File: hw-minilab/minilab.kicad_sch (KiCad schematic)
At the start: 67 parts, among them J1 Screw_Terminal_01x02, J10 Screw_Terminal_01x03, J11 Screw_Terminal_01x03, J12 Conn_01x09_Male, J2 Screw_Terminal_01x02, J3 Conn_01x09_Male, J4 Screw_Terminal_01x04, J5 Screw_Terminal_01x03, J6 Screw_Terminal_01x03, J7 Screw_Terminal_01x03, J8 Screw_Terminal_01x03, J9 Screw_Terminal_01x03, SW1 SW_DPDT_x2, SW2 SW_SPDT, U1 NE555P, U2 L7805, U3 L7833, U4 4069, U5 4069

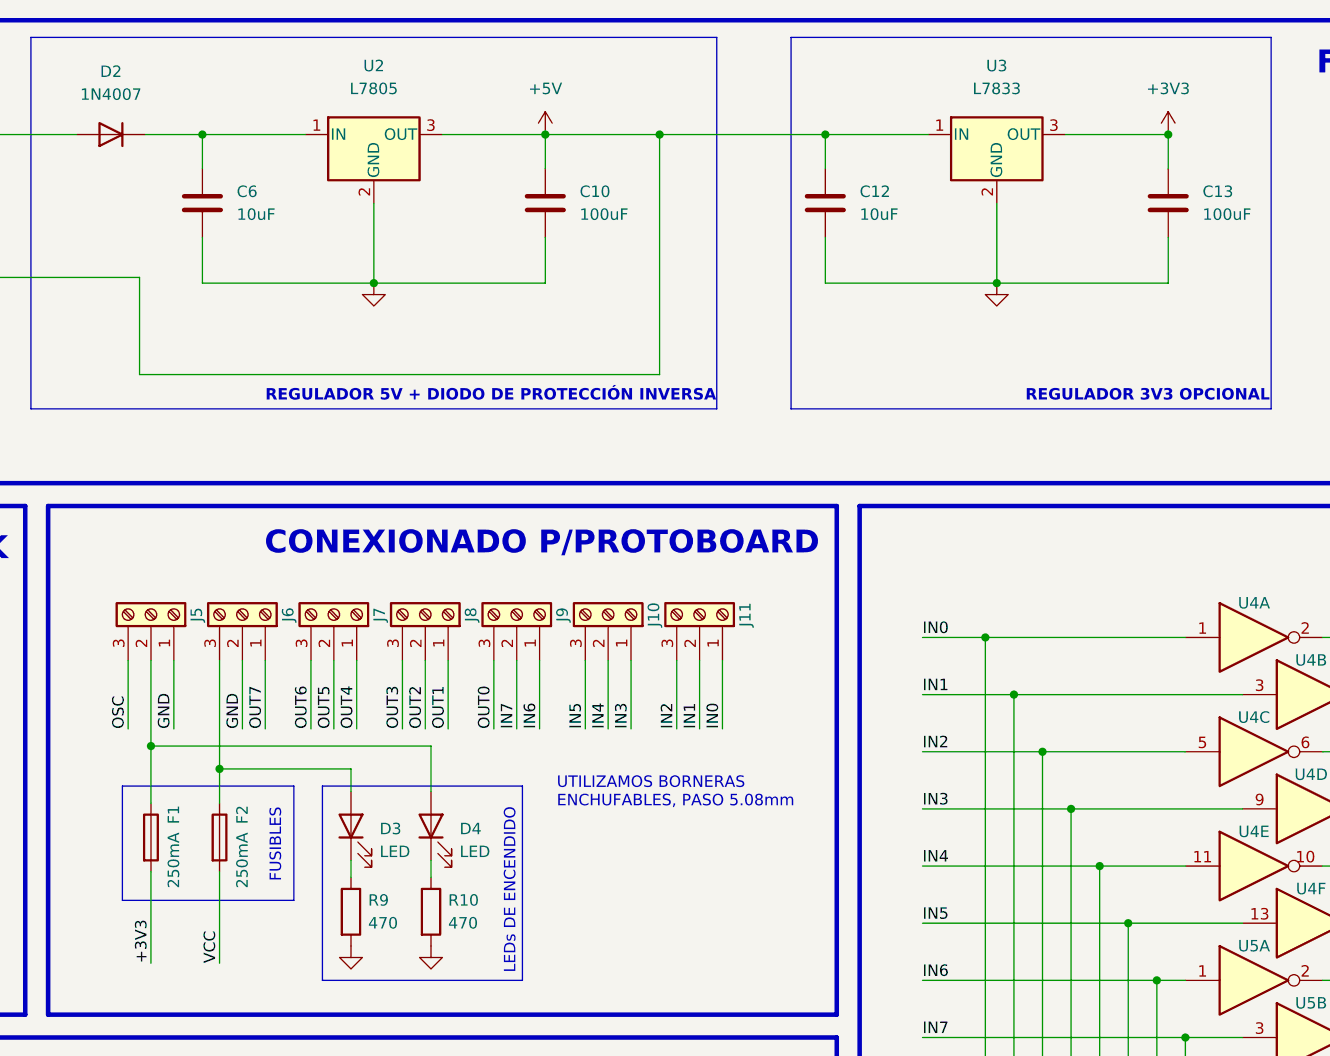
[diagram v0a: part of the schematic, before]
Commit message: Switch 3v3 regulator to kf33
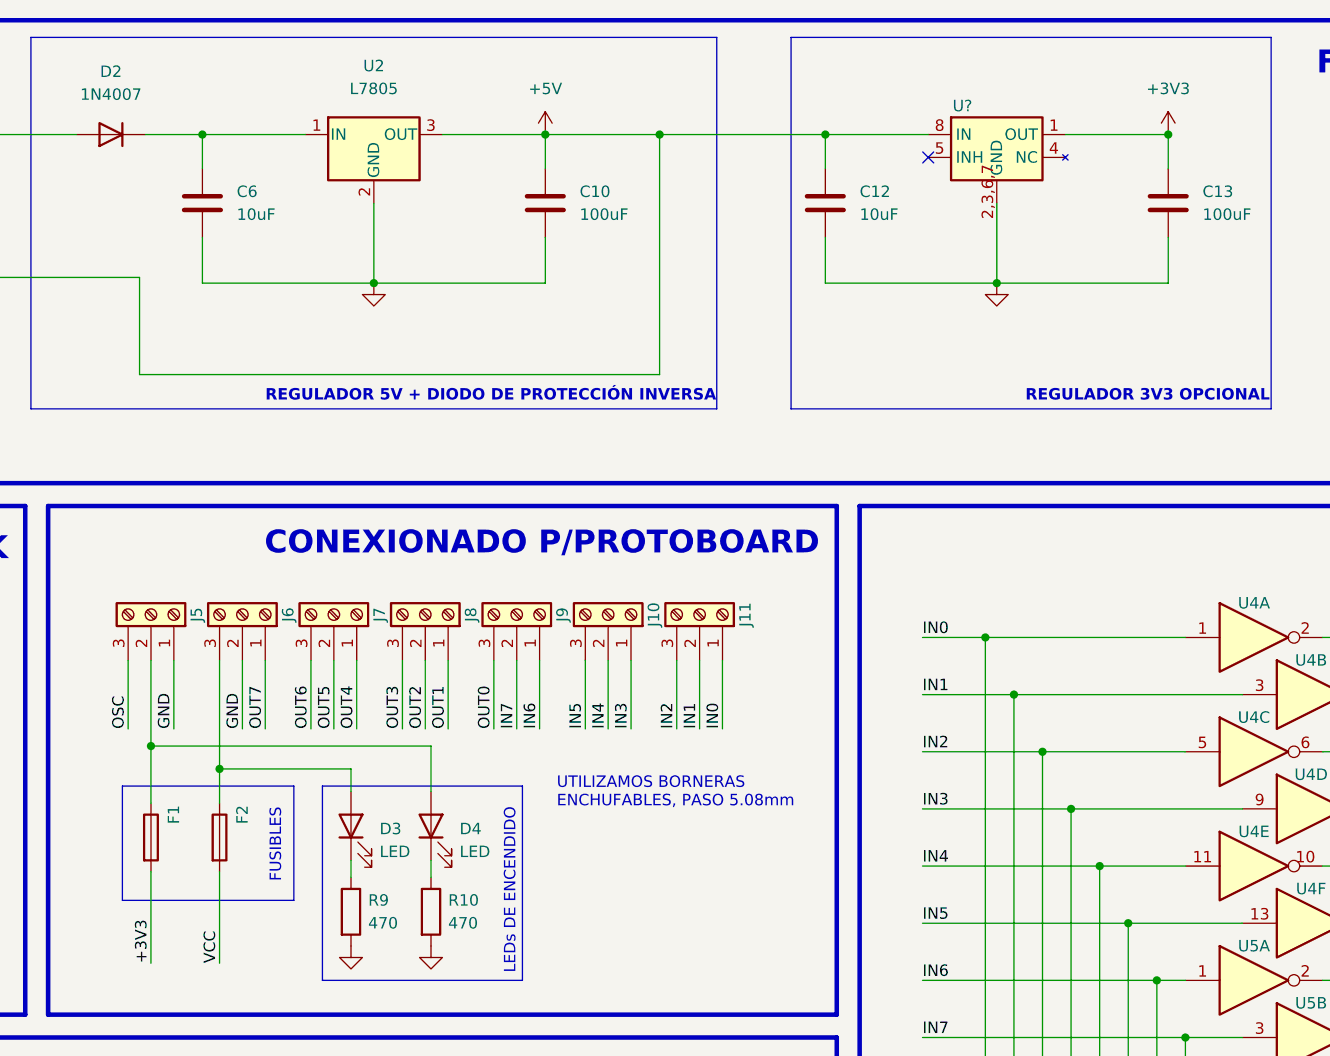
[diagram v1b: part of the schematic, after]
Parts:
- removed U3: L7833, Package_TO_SOT_THT:TO-220-3_Vertical, symbol Regulator_Linear:L7805
- added U?: (no value), symbol lib:KF33
- F1, F2: value 250mA -> (none); footprint TerminalBlock_RND:TerminalBlock_RND_205-00288_1x02_P5.08mm_Horizontal -> (none)
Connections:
- net +3V3: now also U?.1 (OUT)
- net +5V: now also U?.8 (IN)
- net GND: now also U?.2,3,6,7 (GND)
- no-connect marks 3 -> 4
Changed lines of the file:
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@@
   (no_connect (at 53.34 100.965))
   (no_connect (at 27.94 95.885))
+  (no_connect (at 184.785 29.21))
   (no_connect (at 63.5 29.21))
   (polyline (pts (xy 117.475 99.06) (xy 139.7 99.06))
@@
     (stroke (width 0) (type default) (color 0 0 0 0))
   )
+  (wire (pts (xy 200.025 26.67) (xy 211.455 26.67))
+    (stroke (width 0) (type default) (color 0 0 0 0))
+  )
   (wire (pts (xy 253.365 94.615) (xy 267.97 94.615))
     (stroke (width 0) (type default) (color 0 0 0 0))
@@
     (stroke (width 0) (type default) (color 0 0 0 0))
   )
-  (wire (pts (xy 184.785 26.67) (xy 173.355 26.67))
+  (wire (pts (xy 173.355 26.67) (xy 184.785 26.67))
     (stroke (width 0) (type default) (color 0 0 0 0))
   )
@@
     (stroke (width 0) (type default) (color 0 0 0 0))
   )
-  (wire (pts (xy 211.455 26.67) (xy 200.025 26.67))
-    (stroke (width 0) (type default) (color 0 0 0 0))
-  )
   (wire (pts (xy 248.285 107.95) (xy 243.84 107.95))
     (stroke (width 0) (type default) (color 0 0 0 0))
@@
     (pin "1")
   )
-  (symbol (lib_id "Regulator_Linear:L7805") (at 192.405 26.67 0) (unit 1)
-    (in_bom yes) (on_board yes) (fields_autoplaced)
-    (property "Reference" "U3" (id 0) (at 192.405 19.05 0))
-    (property "Value" "L7833" (id 1) (at 192.405 21.59 0))
-    (property "Footprint" "Package_TO_SOT_THT:TO-220-3_Vertical" (id 2) (at 193.04 30.48 0)
-      (effects (font (size 1.27 1.27) italic) (justify left) hide)
+  (symbol (lib_id "lib:KF33") (at 192.405 26.67 0) (unit 1)
+    (in_bom yes) (on_board yes)
+    (property "Reference" "U?" (id 0) (at 188.595 23.495 0))
+    (property "Value" "" (id 1) (at 194.945 23.495 0))
+    (property "Footprint" "" (id 2) (at 192.405 26.67 0)
+      (effects (font (size 1.27 1.27)) hide)
     )
-    (property "Datasheet" "http://www.st.com/content/ccc/resource/technical/document/datasheet/41/4f/b3/b0/12/d4/47/88/CD00000444.pdf/files/CD00000444.pdf/jcr:content/translations/en.CD00000444.pdf" (id 3) (at 192.405 27.94 0)
+    (property "Datasheet" "" (id 3) (at 192.405 26.67 0)
       (effects (font (size 1.27 1.27)) hide)
     )
+    (pin "4")
     (pin "1")
-    (pin "2")
-    (pin "3")
+    (pin "2,3,6,7")
+    (pin "5")
+    (pin "8")
   )
   (symbol (lib_id "Device:R") (at 240.03 127 90) (unit 1)
@@
     (in_bom yes) (on_board yes)
     (property "Reference" "F1" (id 0) (at 100.965 102.235 90))
-    (property "Value" "250mA" (id 1) (at 100.965 107.315 90))
-    (property "Footprint" "TerminalBlock_RND:TerminalBlock_RND_205-00288_1x02_P5.08mm_Horizontal" (id 2) (at 96.647 104.775 90)
+    (property "Value" "" (id 1) (at 100.965 107.315 90))
+    (property "Footprint" "" (id 2) (at 96.647 104.775 90)
       (effects (font (size 1.27 1.27)) hide)
     )
@@
     (in_bom yes) (on_board yes)
     (property "Reference" "F2" (id 0) (at 108.585 102.235 90))
-    (property "Value" "250mA" (id 1) (at 108.585 107.315 90))
-    (property "Footprint" "TerminalBlock_RND:TerminalBlock_RND_205-00288_1x02_P5.08mm_Horizontal" (id 2) (at 104.267 104.775 90)
+    (property "Value" "" (id 1) (at 108.585 107.315 90))
+    (property "Footprint" "" (id 2) (at 104.267 104.775 90)
       (effects (font (size 1.27 1.27)) hide)
     )
@@
     )
     (path "/a3002aff-87e0-400d-bde0-570e1f15484d"
-      (reference "F1") (unit 1) (value "250mA") (footprint "TerminalBlock_RND:TerminalBlock_RND_205-00288_1x02_P5.08mm_Horizontal")
+      (reference "F1") (unit 1) (value "250mA") (footprint "TerminalBlock_Phoenix:TerminalBlock_Phoenix_MKDS-1,5-2-5.08_1x02_P5.08mm_Horizontal")
     )
     (path "/b7c6bafb-aadf-472c-921e-3a8cb7a59ac2"
-      (reference "F2") (unit 1) (value "250mA") (footprint "TerminalBlock_RND:TerminalBlock_RND_205-00288_1x02_P5.08mm_Horizontal")
+      (reference "F2") (unit 1) (value "250mA") (footprint "TerminalBlock_Phoenix:TerminalBlock_Phoenix_MKDS-1,5-2-5.08_1x02_P5.08mm_Horizontal")
     )
     (path "/2dd780f8-df52-4609-ad66-25501efcd296"
@@
       (reference "U2") (unit 1) (value "L7805") (footprint "Package_TO_SOT_THT:TO-220-3_Vertical")
     )
-    (path "/056a54a7-0913-41c5-a754-b3201ec3b595"
-      (reference "U3") (unit 1) (value "L7833") (footprint "Package_TO_SOT_THT:TO-220-3_Vertical")
-    )
     (path "/f245ec42-7b6c-4ad0-aa95-177eeea6ecef"
       (reference "U4") (unit 1) (value "4069") (footprint "Package_DIP:DIP-14_W7.62mm_Socket_LongPads")
@@
       (reference "U5") (unit 7) (value "4069") (footprint "Package_DIP:DIP-14_W7.62mm_Socket_LongPads")
     )
+    (path "/03a24617-13e6-4922-ab6c-5cb103d61f18"
+      (reference "U?") (unit 1) (value "KF33") (footprint "Package_SO:SOIC-8-1EP_3.9x4.9mm_P1.27mm_EP2.29x3mm")
+    )
   )

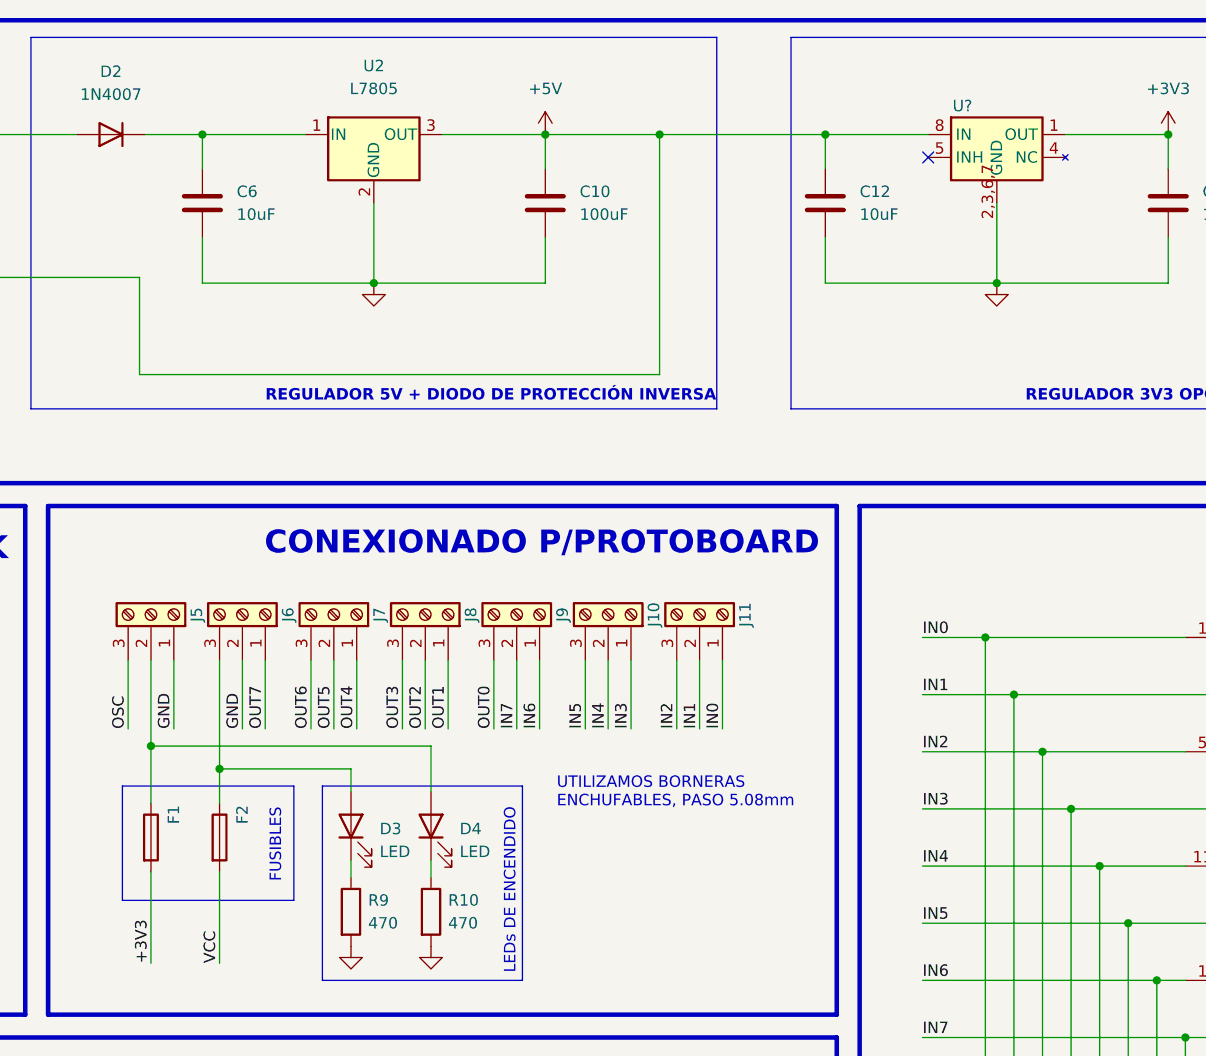
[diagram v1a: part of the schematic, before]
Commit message: Avances en el routeo
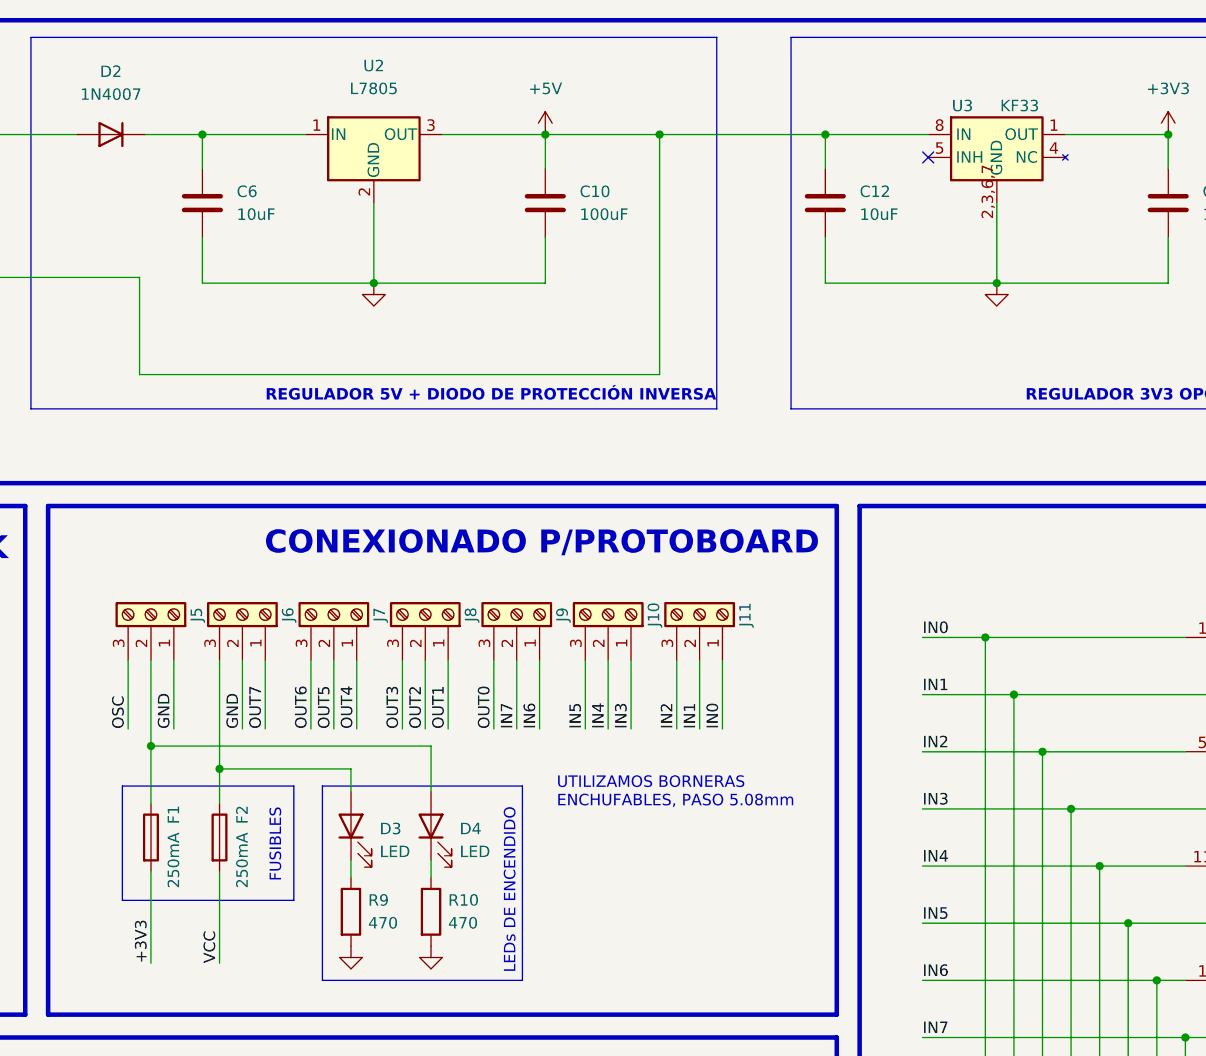
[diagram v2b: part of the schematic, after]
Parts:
- F1, F2: value (none) -> 250mA; footprint (none) -> TerminalBlock_Phoenix:TerminalBlock_Phoenix_MKDS-1,5-2-5.08_1x02_P5.08mm_Horizontal
- U3: renamed from U?; value (none) -> KF33; footprint (none) -> Package_SO:SOIC-8-1EP_3.9x4.9mm_P1.27mm_EP2.29x3mm
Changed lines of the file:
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@@
   (symbol (lib_id "lib:KF33") (at 192.405 26.67 0) (unit 1)
     (in_bom yes) (on_board yes)
-    (property "Reference" "U?" (id 0) (at 188.595 23.495 0))
-    (property "Value" "" (id 1) (at 194.945 23.495 0))
-    (property "Footprint" "" (id 2) (at 192.405 26.67 0)
+    (property "Reference" "U3" (id 0) (at 188.595 23.495 0))
+    (property "Value" "KF33" (id 1) (at 194.945 23.495 0))
+    (property "Footprint" "Package_SO:SOIC-8-1EP_3.9x4.9mm_P1.27mm_EP2.29x3mm" (id 2) (at 192.405 26.67 0)
       (effects (font (size 1.27 1.27)) hide)
     )
@@
     (in_bom yes) (on_board yes)
     (property "Reference" "F1" (id 0) (at 100.965 102.235 90))
-    (property "Value" "" (id 1) (at 100.965 107.315 90))
-    (property "Footprint" "" (id 2) (at 96.647 104.775 90)
+    (property "Value" "250mA" (id 1) (at 100.965 107.315 90))
+    (property "Footprint" "TerminalBlock_Phoenix:TerminalBlock_Phoenix_MKDS-1,5-2-5.08_1x02_P5.08mm_Horizontal" (id 2) (at 96.647 104.775 90)
       (effects (font (size 1.27 1.27)) hide)
     )
@@
     (in_bom yes) (on_board yes)
     (property "Reference" "F2" (id 0) (at 108.585 102.235 90))
-    (property "Value" "" (id 1) (at 108.585 107.315 90))
-    (property "Footprint" "" (id 2) (at 104.267 104.775 90)
+    (property "Value" "250mA" (id 1) (at 108.585 107.315 90))
+    (property "Footprint" "TerminalBlock_Phoenix:TerminalBlock_Phoenix_MKDS-1,5-2-5.08_1x02_P5.08mm_Horizontal" (id 2) (at 104.267 104.775 90)
       (effects (font (size 1.27 1.27)) hide)
     )
@@
       (reference "U2") (unit 1) (value "L7805") (footprint "Package_TO_SOT_THT:TO-220-3_Vertical")
     )
+    (path "/03a24617-13e6-4922-ab6c-5cb103d61f18"
+      (reference "U3") (unit 1) (value "KF33") (footprint "Package_SO:SOIC-8-1EP_3.9x4.9mm_P1.27mm_EP2.29x3mm")
+    )
     (path "/f245ec42-7b6c-4ad0-aa95-177eeea6ecef"
       (reference "U4") (unit 1) (value "4069") (footprint "Package_DIP:DIP-14_W7.62mm_Socket_LongPads")
@@
       (reference "U5") (unit 7) (value "4069") (footprint "Package_DIP:DIP-14_W7.62mm_Socket_LongPads")
     )
-    (path "/03a24617-13e6-4922-ab6c-5cb103d61f18"
-      (reference "U?") (unit 1) (value "KF33") (footprint "Package_SO:SOIC-8-1EP_3.9x4.9mm_P1.27mm_EP2.29x3mm")
-    )
-  )
+  )

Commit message: Archivos de fabricacion generados
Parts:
- removed J4: Screw_Terminal_01x04, TerminalBlock_Phoenix:TerminalBlock_Phoenix_MKDS-1,5-4-5.08_1x04_P5.08mm_Horizontal, symbol Connector:Screw_Terminal_01x04
- removed SW2: SW_SPDT, Connector_PinHeader_2.54mm:PinHeader_1x03_P2.54mm_Vertical, symbol Switch:SW_SPDT
- added H1, H3, H4: MountingHole, MountingHole:MountingHole_3.2mm_M3, symbol Mechanical:MountingHole
- added H2: (no value), symbol Mechanical:MountingHole
- added J4, J5: Screw_Terminal_01x02, TestPoint:TestPoint_2Pads_Pitch5.08mm_Drill1.3mm, symbol Connector:Screw_Terminal_01x02
- added unit 4 of U5
- added unit 6 of U5
- added unit 5 of U5
- added unit 3 of U5
- F1, F2: value 250mA -> (none); footprint TerminalBlock_Phoenix:TerminalBlock_Phoenix_MKDS-1,5-2-5.08_1x02_P5.08mm_Horizontal -> (none)
- J1, J2: value Screw_Terminal_01x02 -> (none); footprint TerminalBlock_Phoenix:TerminalBlock_Phoenix_MKDS-1,5-2-5.08_1x02_P5.08mm_Horizontal -> (none)
- SW1: value SW_DPDT_x2 -> (none); footprint Connector_PinHeader_2.54mm:PinHeader_2x03_P2.54mm_Vertical -> (none)
- U2: value L7805 -> (none); footprint Package_TO_SOT_THT:TO-220-3_Vertical -> (none)
- U3: value KF33 -> (none)
- U4, U5: value 4069 -> (none); footprint Package_DIP:DIP-14_W7.62mm_Socket_LongPads -> (none)
- renumbered J9 to J10, J10 to J11, J11 to J12, J12 to J13, J5 to J6, J6 to J7, J7 to J8, J8 to J9
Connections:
- net GND: now also D3.1 (K), D4.1 (K), U3.2 (GND), U3.3 (GND), U3.6 (GND), U3.7 (GND), U3.9 (GND), J4.1 (Pin_1), J5.1 (Pin_1); no longer R10.2, R9.2, U3.2,3,6,7 (GND)
- net IN1: now also U4.13
- net IN2: now also U4.11
- net IN4: now also U5.1; no longer U4.11
- net IN5: now also U5.3, U5.13; no longer U4.13
- net IN6: now also U5.11, U5.5; no longer U5.1
- net IN7: now also U5.9; no longer U5.3
- net at R28.1: now also U5.8; no longer U5.4
- net at R9.1: now also F2.1, J7.3 (Pin_3); no longer D3.1 (K)
- net at R27.1: now also U5.6; no longer U5.2
- net at J2.1 (Pin_1), SW1.4 (A): now also J4.2 (Pin_2)
- net at SW1.6 (C): now also J5.2 (Pin_2)
- net at R10.1: now also F1.1, J6.2 (Pin_2); no longer D4.1 (K)
- net at U4.12: no longer R26.1
- net at U4.10: no longer R25.1
- new net: D3.2 (A), R9.2
- new net: R26.1, U5.4
- new net: D4.2 (A), R10.2
- new net: R25.1, U5.2
- no-connect marks 4 -> 8
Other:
- moved on the sheet: D3, D4, R10, R9

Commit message: Version entregada
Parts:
- added SW2: SW_SPDT, Library:TestPoint_3Pads_Pitch5.08mm_Drill1.3mm, symbol Switch:SW_SPDT
- F1, F2: value (none) -> 250mA; footprint (none) -> TestPoint:TestPoint_2Pads_Pitch5.08mm_Drill1.3mm
- H2: value (none) -> MountingHole; footprint (none) -> MountingHole:MountingHole_3.2mm_M3
- J1, J2: value (none) -> Screw_Terminal_01x02; footprint (none) -> TestPoint:TestPoint_2Pads_Pitch5.08mm_Drill1.3mm
- R1, R11, R12, R3, R5, R6, R7, R8: value 10k -> 1k
- SW1: value (none) -> SW_DPDT_x2; footprint (none) -> Library:TestPoint_6Pads_Pitch5.08mm_Drill1.3mm
- U2: value (none) -> L7805; footprint (none) -> Package_TO_SOT_THT:TO-220-3_Horizontal_TabUp
- U3: value (none) -> KF33
- U4, U5: value (none) -> 4069
- U4, U5: value (none) -> 4069; footprint (none) -> Package_DIP:DIP-14_W7.62mm_Socket_LongPads
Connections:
- net +3V3: now also SW2.3 (C)
- net +5V: now also SW2.1 (A)
- net VCC: now also SW2.2 (B)
- net at C2.1, RV1.3, U1.2 (TR): now also U1.6 (THR)
- no-connect marks 8 -> 7
